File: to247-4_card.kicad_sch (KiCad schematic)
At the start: 0 parts

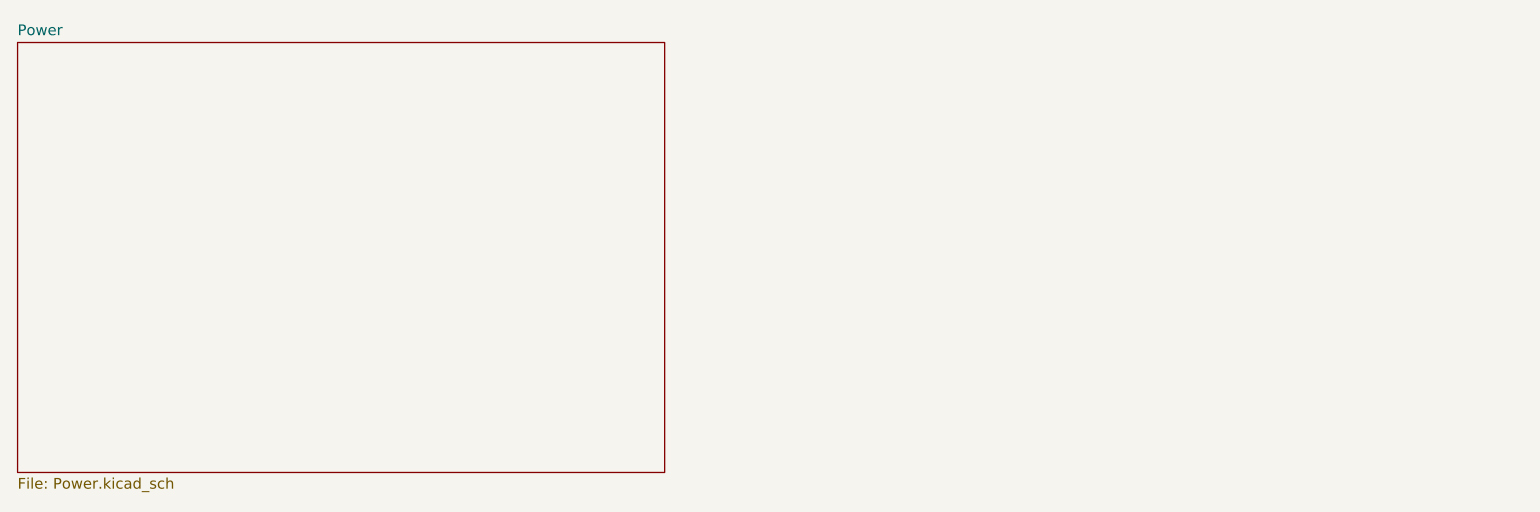
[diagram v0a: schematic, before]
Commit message: started gate drive for top fet
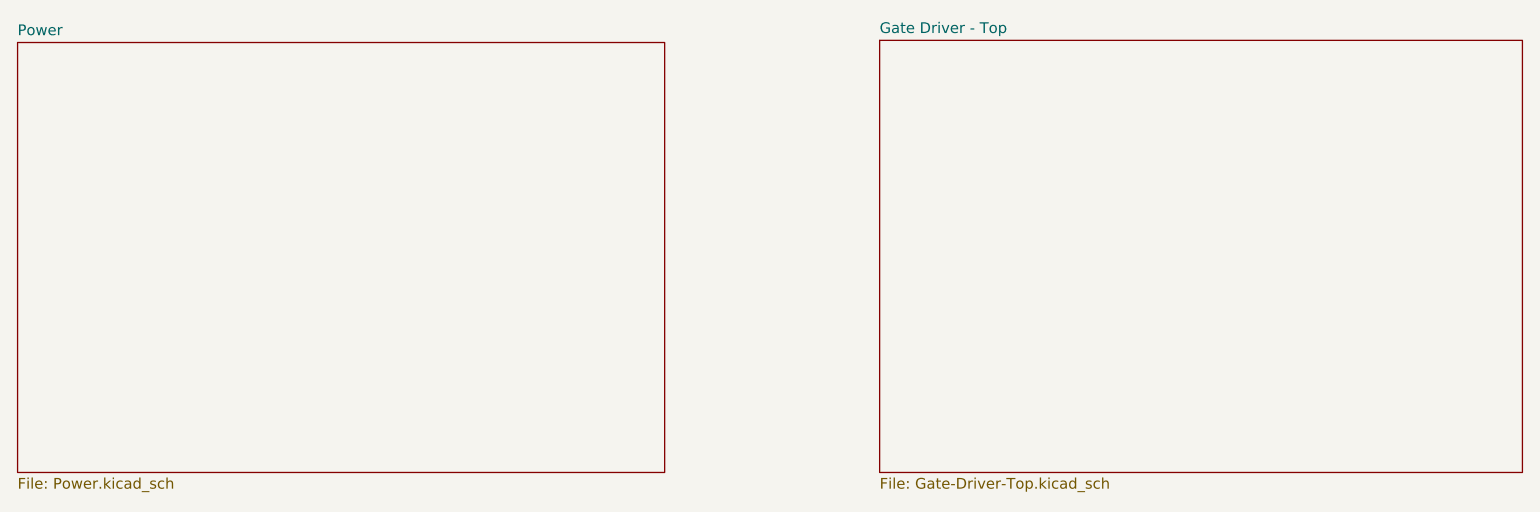
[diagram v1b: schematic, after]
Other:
- added sheet Gate Driver - Top (Gate-Driver-Top.kicad_sch)
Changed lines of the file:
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@@
 	(paper "A4")
+	(sheet
+		(at 127.254 25.146)
+		(size 75.946 51.054)
+		(exclude_from_sim no)
+		(in_bom yes)
+		(on_board yes)
+		(dnp no)
+		(fields_autoplaced yes)
+		(stroke
+			(width 0.1524)
+			(type solid)
+		)
+		(fill
+			(color 0 0 0 0.0000)
+		)
+		(property "Sheetname" "Gate Driver - Top"
+			(at 127.254 24.4344 0)
+			(effects
+				(font
+					(size 1.27 1.27)
+				)
+				(justify left bottom)
+			)
+		)
+		(property "Sheetfile" "Gate-Driver-Top.kicad_sch"
+			(at 127.254 76.7846 0)
+			(effects
+				(font
+					(size 1.27 1.27)
+				)
+				(justify left top)
+			)
+		)
+		(instances
+			(project "to247-4_card"
+				(path "/b6582af5-6107-4ea5-94ab-56651da9db37"
+					(page "3")
+				)
+			)
+		)
+	)
 	(sheet
 		(at 25.4 25.4)

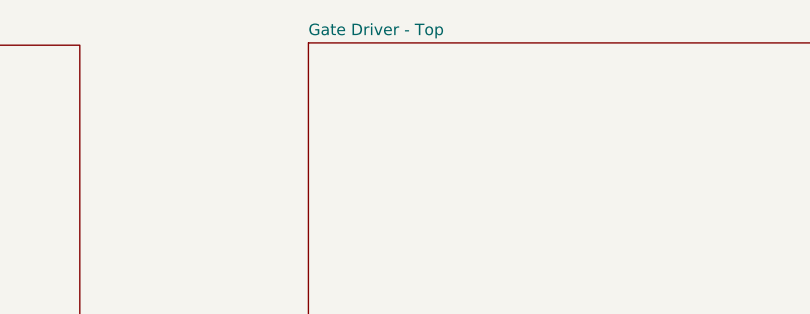
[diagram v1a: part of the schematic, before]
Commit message: gate driver added
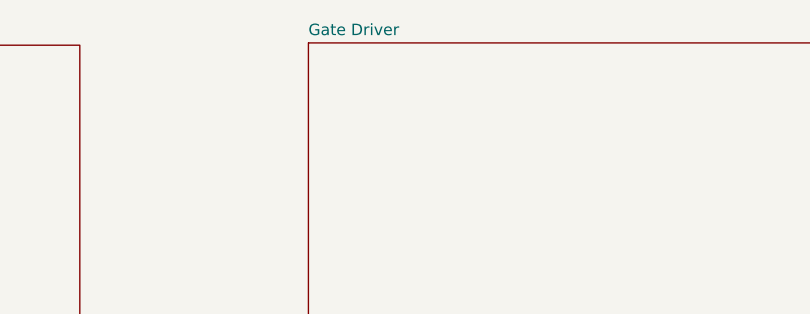
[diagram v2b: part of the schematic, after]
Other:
- sheet Gate Driver - Top renamed Gate Driver
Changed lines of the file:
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@@
 			(color 0 0 0 0.0000)
 		)
-		(property "Sheetname" "Gate Driver - Top"
+		(property "Sheetname" "Gate Driver"
 			(at 127.254 24.4344 0)
 			(effects
